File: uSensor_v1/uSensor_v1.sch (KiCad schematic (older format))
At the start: 224 parts, among them J1 +12V Supply, J2 Conn_01x03, J3 Conn_01x03, J4 NS25-W8P 6-pin 2,54mm, J5 USB_B, J6 GNDA-GNDD Jumper, Q1 BC817-25, Q2 BC817-25, SW1 SW_Push, SW2 SW_Push, U1 AM10TW-2405DZ, U10 KSS-213, U11 AD7795, U12 AD5667, U13 TBD, U15 REF192, U2 LD1117A, U22 RCLAMP, U3 STM32F407VGTx, U4 MCP9700AT, U5 MCP9700AT, U6 LM6132A, U7 MCP9700AT, U8 MCP9700AT, U9 UG-2864KSWLG01

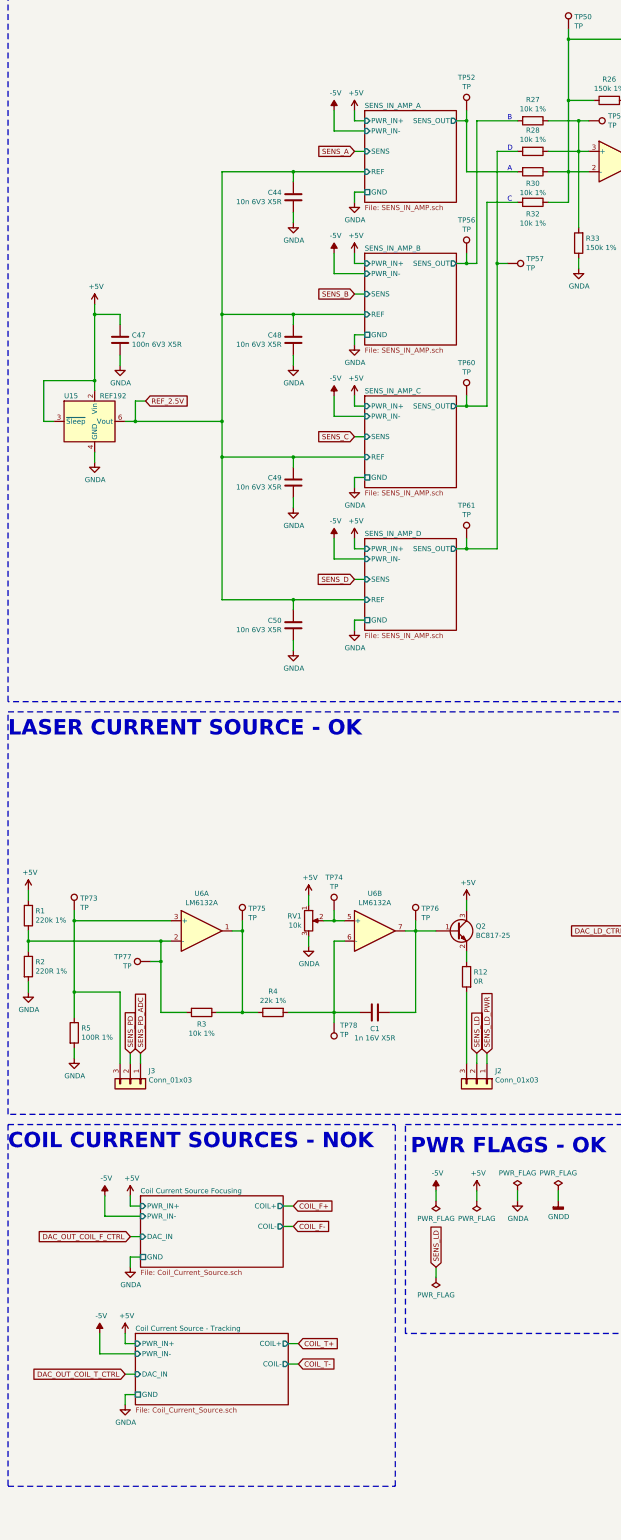
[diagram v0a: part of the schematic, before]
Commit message: Schematic changed (added 2channel opamp in one HS)
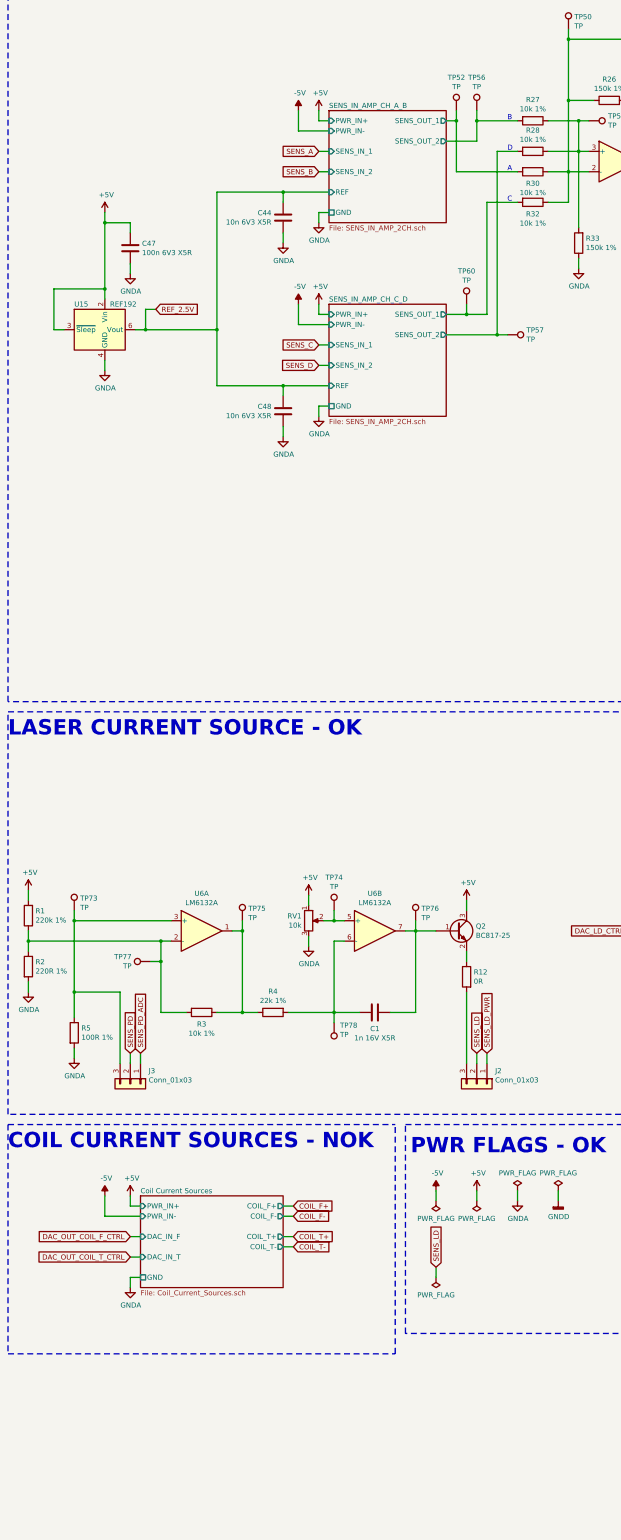
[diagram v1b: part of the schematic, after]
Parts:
- removed C49, C50: 10n 6V3 X5R, Capacitor_SMD:C_0603_1608Metric_Pad1.05x0.95mm_HandSolder, symbol Device:C
- removed TP61: TP, Sentisa-Connectors:TestPoint_Probe_1.0mmDiameter_0.6mmDrill, symbol Connector:TestPoint
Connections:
- net SENS_IN_AMP_A/SENS_OUT renamed SENS_IN_AMP_CH_A_B/SENS_OUT_1
- net SENS_IN_AMP_B/SENS_OUT renamed SENS_IN_AMP_CH_A_B/SENS_OUT_2
- net SENS_IN_AMP_C/SENS_OUT renamed SENS_IN_AMP_CH_C_D/SENS_OUT_1
- net SENS_IN_AMP_D/SENS_OUT renamed SENS_IN_AMP_CH_C_D/SENS_OUT_2
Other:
- moved on the sheet: C47, TP52, TP56, TP57, TP60, U15

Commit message: Layout in progress.
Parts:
- removed C44, C48: 10n 6V3 X5R, Capacitor_SMD:C_0603_1608Metric_Pad1.05x0.95mm_HandSolder, symbol Device:C
- added J7: Barrel_Jack_Switch, Connector_BarrelJack:BarrelJack_Wuerth_6941xx301002, symbol Connector:Barrel_Jack_Switch
- U10: value KSS-213 -> KSS-213 Connector; footprint TBD -> Marcel -> Connector_FFC-FPC:TE_1-84952-6_1x16-1MP_P1.0mm_Horizontal; MFR Sony -> TBD (Sony); MPN KSS-213C -> (TDB) KSS-213C
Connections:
- net at D1.2 (A), J1.1 (Pin_1), TP3.1: now also J7.1
- net at C11.2, C12.2, D3.2 (A2)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: now also J7.2, J7.3
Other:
- moved on the sheet: C1, C11, C12, C19, D1, D3, J1, J2, J3, L2, Q1, Q2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

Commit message: Layout in progress.
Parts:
- added R75: 100k, Resistor_SMD:R_0603_1608Metric_Pad1.05x0.95mm_HandSolder, symbol Device:R
- added SW3: SW_Push, Button_Switch_THT:SW_PUSH_6mm_H4.3mm, symbol Switch:SW_Push
- U10: footprint Connector_FFC-FPC:TE_1-84952-6_1x16-1MP_P1.0mm_Horizontal -> Sentisa-Connectors:Molex_52271-1679_1x16_1mm_Pitch_FFC_FPC_Horizontal_SMT
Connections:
- net +3V3: now also R75.2
- net GNDD: now also SW3.2
- net PROG_~RST: now also R75.1, SW3.1
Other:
- moved on the sheet: C13, C16, C17, C20, C4, C5, C6, C67, C7, C8, D5, D6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

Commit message: Layout in progress.
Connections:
- net FOC_ERR_2_ADC: now also R70.1; no longer R73.1
- net SENS_B: now also R73.1; no longer R68.1
- net SENS_C: now also R74.1; no longer R69.1
- net SENS_D: now also R68.1; no longer R70.1
- net SENS_PD: now also R69.1; no longer R74.1
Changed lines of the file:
@@
 FT
 NoConn ~ 13600 5450
-Text GLabel 12750 13850 0    50   Input ~ 0
+Text GLabel 11200 16850 0    50   Input ~ 0
 FOC_ERR_2_ADC
 $Comp
@@
 Text GLabel 11200 13850 0    50   Input ~ 0
 SENS_A
+Text GLabel 12750 13850 0    50   Input ~ 0
+SENS_B
+Text GLabel 12450 16450 0    50   Input ~ 0
+SENS_C
 Text GLabel 11200 14850 0    50   Input ~ 0
-SENS_B
-Text GLabel 11200 15850 0    50   Input ~ 0
-SENS_C
-Text GLabel 11200 16850 0    50   Input ~ 0
 SENS_D
 Wire Wire Line
@@
 	14750 16250 14750 15950
 Connection ~ 14750 15950
-Text GLabel 12450 16450 0    50   Input ~ 0
+Text GLabel 11200 15850 0    50   Input ~ 0
 SENS_PD
 Wire Wire Line

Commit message: Layout in progress.
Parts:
- removed TP22: TP, Sentisa-Connectors:TestPoint_Probe_1.0mmDiameter_0.6mmDrill, symbol Connector:TestPoint
- added CS1, CS2, CS3: Curr_Sens, Sentisa-Connectors:Current_Sense_Pin_Header_SMD_Pitch1.27mm, symbol Device:Jumper_NC_Small
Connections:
- net ADC_~CS: now also U3.77 (JTDI/SPI3_NSS/I2S3_WS/TIM2_CH1_ETR/SPI1_NSS/EVENTOUT/PA15); no longer U3.66 (I2S_CKIN/MCO2/TIM8_CH4/SDIO_D1/I2C3_SDA/DCMI_D3/TIM3_CH4/EVENTOUT/PC9)
- net COIL_F+: now also CS1.1; no longer U10.13 (F+)
- net COIL_T+: now also CS2.1; no longer U10.14 (T+)
- net DAC_OUT_COIL_F_CTRL: now also U12.1 (VOUT_A); no longer U12.2 (VOUT_B)
- net DAC_OUT_COIL_T_CTRL: now also U12.2 (VOUT_B); no longer U12.1 (VOUT_A)
- net DAC_~LDAC: now also TP21.1
- net SENS_LD: now also CS3.1; no longer L4.1
- net at R9.1, U3.97 (PE0/TIM4_ETR/FSMC_NBL0/DCMI_D2/EVENTOUT): no longer TP21.1
- new net: CS1.2, U10.13 (F+)
- new net: CS3.2, L4.1
- new net: CS2.2, U10.14 (T+)
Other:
- moved on the sheet: C42, L4, TP27, TP28, TP29, TP30, TP31, TP32

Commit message: Connection done.
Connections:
- net +3V3: no longer C21.1, C22.1, C23.1, C24.1, U4.1 (Vdd), U5.1 (Vdd), U7.1 (Vdd), U8.1 (Vdd)
- net +5V: now also C21.1, C22.1, C23.1, C24.1, U4.1 (Vdd), U5.1 (Vdd), U7.1 (Vdd), U8.1 (Vdd)
- net GNDA: now also C21.2, C22.2, C23.2, C24.2, U4.3 (GND), U5.3 (GND), U7.3 (GND), U8.3 (GND)
- net GNDD: no longer C21.2, C22.2, C23.2, C24.2, U4.3 (GND), U5.3 (GND), U7.3 (GND), U8.3 (GND)
- net TEMP_SENS_OUT_1: now also U7.2 (Vout); no longer U4.2 (Vout)
- net TEMP_SENS_OUT_2: now also U4.2 (Vout); no longer U7.2 (Vout)
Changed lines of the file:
@@
 	13200 9900 13200 9800
 $Comp
-L power:+3V3 #PWR08
+L power:+5V #PWR08
 U 1 1 5DA192D4
 P 13200 9000
 F 0 "#PWR08" H 13200 8850 50  0001 C CNN
-F 1 "+3V3" H 13215 9173 50  0000 C CNN
+F 1 "+5V" H 13215 9173 50  0000 C CNN
 F 2 "" H 13200 9000 50  0001 C CNN
 F 3 "" H 13200 9000 50  0001 C CNN
@@
 	13200 9200 13200 9100
 Connection ~ 13200 9100
-Text GLabel 13800 9500 2    40   Output ~ 0
+Text GLabel 13700 11100 2    40   Output ~ 0
 TEMP_SENS_OUT_1
 Wire Wire Line
@@
 $EndComp
 $Comp
-L power:GNDD #PWR017
+L power:GNDA #PWR017
 U 1 1 5DAE0233
 P 13200 11600
 F 0 "#PWR017" H 13200 11350 50  0001 C CNN
-F 1 "GNDD" H 13205 11427 50  0000 C CNN
+F 1 "GNDA" H 13205 11427 50  0000 C CNN
 F 2 "" H 13200 11600 50  0001 C CNN
 F 3 "" H 13200 11600 50  0001 C CNN
@@
 	13200 11500 13200 11400
 $Comp
-L power:+3V3 #PWR015
+L power:+5V #PWR015
 U 1 1 5DAE023E
 P 13200 10600
 F 0 "#PWR015" H 13200 10450 50  0001 C CNN
-F 1 "+3V3" H 13215 10773 50  0000 C CNN
+F 1 "+5V" H 13215 10773 50  0000 C CNN
 F 2 "" H 13200 10600 50  0001 C CNN
 F 3 "" H 13200 10600 50  0001 C CNN
@@
 	13200 10800 13200 10700
 Connection ~ 13200 10700
-Text GLabel 13700 11100 2    40   Output ~ 0
+Text GLabel 13800 9500 2    40   Output ~ 0
 TEMP_SENS_OUT_2
 Wire Wire Line
@@
 	15550 9900 15550 9800
 $Comp
-L power:+3V3 #PWR09
+L power:+5V #PWR09
 U 1 1 5DB14C16
 P 15550 9000
 F 0 "#PWR09" H 15550 8850 50  0001 C CNN
-F 1 "+3V3" H 15565 9173 50  0000 C CNN
+F 1 "+5V" H 15565 9173 50  0000 C CNN
 F 2 "" H 15550 9000 50  0001 C CNN
 F 3 "" H 15550 9000 50  0001 C CNN
@@
 $EndComp
 $Comp
-L power:GNDD #PWR018
+L power:GNDA #PWR018
 U 1 1 5DB14C31
 P 15550 11600
 F 0 "#PWR018" H 15550 11350 50  0001 C CNN
-F 1 "GNDD" H 15555 11427 50  0000 C CNN
+F 1 "GNDA" H 15555 11427 50  0000 C CNN
 F 2 "" H 15550 11600 50  0001 C CNN
 F 3 "" H 15550 11600 50  0001 C CNN
@@
 	15550 11500 15550 11400
 $Comp
-L power:+3V3 #PWR016
+L power:+5V #PWR016
 U 1 1 5DB14C3C
 P 15550 10600
 F 0 "#PWR016" H 15550 10450 50  0001 C CNN
-F 1 "+3V3" H 15565 10773 50  0000 C CNN
+F 1 "+5V" H 15565 10773 50  0000 C CNN
 F 2 "" H 15550 10600 50  0001 C CNN
 F 3 "" H 15550 10600 50  0001 C CNN
@@
 $EndComp
 $Comp
-L power:GNDD #PWR014
+L power:GNDA #PWR014
 U 1 1 5DB14C0B
 P 15550 10000
 F 0 "#PWR014" H 15550 9750 50  0001 C CNN
-F 1 "GNDD" H 15555 9827 50  0000 C CNN
+F 1 "GNDA" H 15555 9827 50  0000 C CNN
 F 2 "" H 15550 10000 50  0001 C CNN
 F 3 "" H 15550 10000 50  0001 C CNN
@@
 $EndComp
 $Comp
-L power:GNDD #PWR0156
+L power:GNDA #PWR0156
 U 1 1 5D33AE3D
 P 13200 10000
 F 0 "#PWR0156" H 13200 9750 50  0001 C CNN
-F 1 "GNDD" H 13204 9845 50  0000 C CNN
+F 1 "GNDA" H 13204 9845 50  0000 C CNN
 F 2 "" H 13200 10000 50  0001 C CNN
 F 3 "" H 13200 10000 50  0001 C CNN

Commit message: Layout ready to 1st review.
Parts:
- J1: footprint Connector_PinHeader_2.54mm:PinHeader_1x02_P2.54mm_Vertical -> Connector_Molex:Molex_KK-254_AE-6410-02A_1x02_P2.54mm_Vertical
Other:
- moved on the sheet: C11, D1, D3, J1, J7, TP3, TP4
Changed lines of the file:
@@
 L Connector_Generic:Conn_01x02 J1
 U 1 1 5C42724A
-P 850 2200
-F 0 "J1" V 1150 2150 50  0000 C CNN
-F 1 "+12V Supply" V 1050 2150 50  0000 C CNN
-F 2 "Connector_PinHeader_2.54mm:PinHeader_1x02_P2.54mm_Vertical" H 850 2200 50  0001 C CNN
-F 3 "~" H 850 2200 50  0001 C CNN
-F 4 "Main Supply Connector" V 950 2150 50  0000 C CNN "Function"
-	1    850  2200
+P 1000 2200
+F 0 "J1" V 1300 2150 50  0000 C CNN
+F 1 "+12V Supply" V 1200 2150 50  0000 C CNN
+F 2 "Connector_Molex:Molex_KK-254_AE-6410-02A_1x02_P2.54mm_Vertical" H 1000 2200 50  0001 C CNN
+F 3 "~" H 1000 2200 50  0001 C CNN
+F 4 "Main Supply Connector" V 1100 2150 50  0000 C CNN "Function"
+	1    1000 2200
 	-1   0    0    -1
 $EndComp
@@
 L Device:C C11
 U 1 1 5C427492
-P 2200 2250
-F 0 "C11" H 2315 2296 50  0000 L CNN
-F 1 "2u2 50V X5R" H 2315 2205 50  0000 L CNN
-F 2 "Resistor_SMD:R_0805_2012Metric_Pad1.15x1.40mm_HandSolder" H 2238 2100 50  0001 C CNN
-F 3 "~" H 2200 2250 50  0001 C CNN
-	1    2200 2250
+P 2250 2250
+F 0 "C11" H 2365 2296 50  0000 L CNN
+F 1 "2u2 50V X5R" H 2365 2205 50  0000 L CNN
+F 2 "Resistor_SMD:R_0805_2012Metric_Pad1.15x1.40mm_HandSolder" H 2288 2100 50  0001 C CNN
+F 3 "~" H 2250 2250 50  0001 C CNN
+	1    2250 2250
 	1    0    0    -1
 $EndComp
@@
 	3000 2500 3000 2400
 Wire Wire Line
-	2200 2500 2200 2400
+	2250 2500 2250 2400
 Wire Wire Line
-	1050 2300 1350 2300
+	1200 2300 1400 2300
 Wire Wire Line
-	1450 2300 1450 2500
-Connection ~ 2200 2500
+	1500 2300 1500 2500
+Connection ~ 2250 2500
 Wire Wire Line
-	1050 2200 1250 2200
+	1200 2200 1300 2200
 Wire Wire Line
-	1450 2200 1450 2000
+	1500 2200 1500 2000
 Wire Wire Line
-	2200 2000 2200 2100
+	2250 2000 2250 2100
 Wire Wire Line
-	2500 2000 2200 2000
+	2500 2000 2250 2000
 Wire Wire Line
 	2800 2000 3000 2000
@@
 L Device:D_Schottky D1
 U 1 1 5CAE2AA1
-P 1700 2000
-F 0 "D1" H 1700 1784 50  0000 C CNN
-F 1 "40V 2A" H 1700 1875 50  0000 C CNN
-F 2 "Sentisa-Diodes:D_SMB" H 1700 2000 50  0001 C CNN
-F 3 "~" H 1700 2000 50  0001 C CNN
-F 4 "Diotec Semiconductor" H 1700 2000 50  0001 C CNN "MFR"
-F 5 "SK25" H 1700 2000 50  0001 C CNN "MPN"
-	1    1700 2000
+P 1750 2000
+F 0 "D1" H 1750 1784 50  0000 C CNN
+F 1 "40V 2A" H 1750 1875 50  0000 C CNN
+F 2 "Sentisa-Diodes:D_SMB" H 1750 2000 50  0001 C CNN
+F 3 "~" H 1750 2000 50  0001 C CNN
+F 4 "Diotec Semiconductor" H 1750 2000 50  0001 C CNN "MFR"
+F 5 "SK25" H 1750 2000 50  0001 C CNN "MPN"
+	1    1750 2000
 	-1   0    0    1
 $EndComp
 Wire Wire Line
-	1850 2000 1950 2000
-Connection ~ 2200 2000
+	1900 2000 2000 2000
+Connection ~ 2250 2000
 $Comp
 L Device:R R6
@@
 L Diode:1.5KExxA D3
 U 1 1 5E6A365E
-P 1950 2250
-F 0 "D3" V 1904 2172 50  0000 R CNN
-F 1 "TVS 40V" V 1995 2172 50  0000 R CNN
-F 2 "Sentisa-Diodes:D_SMB" H 1950 2050 50  0001 C CNN
-F 3 "" H 1900 2250 50  0001 C CNN
-F 4 "Vishay" V 1950 2250 50  0001 C CNN "MPN"
-F 5 "SMBJ40D-M3/H" V 1950 2250 50  0001 C CNN "MFR"
-	1    1950 2250
+P 2000 2250
+F 0 "D3" V 1954 2172 50  0000 R CNN
+F 1 "TVS 40V" V 2045 2172 50  0000 R CNN
+F 2 "Sentisa-Diodes:D_SMB" H 2000 2050 50  0001 C CNN
+F 3 "" H 1950 2250 50  0001 C CNN
+F 4 "Vishay" V 2000 2250 50  0001 C CNN "MPN"
+F 5 "SMBJ40D-M3/H" V 2000 2250 50  0001 C CNN "MFR"
+	1    2000 2250
 	0    1    1    0
 $EndComp
 Wire Wire Line
-	1450 2000 1550 2000
+	1500 2000 1600 2000
 Wire Wire Line
-	1450 2500 1950 2500
+	1500 2500 2000 2500
 Wire Wire Line
-	1950 2100 1950 2000
-Connection ~ 1950 2000
+	2000 2100 2000 2000
+Connection ~ 2000 2000
 Wire Wire Line
-	1950 2000 2200 2000
+	2000 2000 2250 2000
 Wire Wire Line
-	1950 2400 1950 2500
-Connection ~ 1950 2500
+	2000 2400 2000 2500
+Connection ~ 2000 2500
 Text GLabel 8400 14650 2    50   Output ~ 0
 DAC_OUT_COIL_T_CTRL
 Wire Wire Line
-	1950 2500 2200 2500
+	2000 2500 2250 2500
 Wire Wire Line
-	2200 2500 3000 2500
+	2250 2500 3000 2500
 Wire Wire Line
 	20750 5550 20950 5550
@@
 L Connector:TestPoint TP3
 U 1 1 5C3E6779
-P 1450 1900
-F 0 "TP3" H 1450 2225 50  0000 C CNN
-F 1 "TP" H 1450 2134 50  0000 C CNN
-F 2 "Sentisa-Connectors:TestPoint_Probe_1.0mmDiameter_0.6mmDrill" H 1650 1900 50  0001 C CNN
-F 3 "~" H 1650 1900 50  0001 C CNN
-	1    1450 1900
+P 1500 1900
+F 0 "TP3" H 1500 2225 50  0000 C CNN
+F 1 "TP" H 1500 2134 50  0000 C CNN
+F 2 "Sentisa-Connectors:TestPoint_Probe_1.0mmDiameter_0.6mmDrill" H 1700 1900 50  0001 C CNN
+F 3 "~" H 1700 1900 50  0001 C CNN
+	1    1500 1900
 	1    0    0    -1
 $EndComp
@@
 L Connector:TestPoint TP4
 U 1 1 5C459570
-P 1450 2600
-F 0 "TP4" H 1392 2627 50  0000 R CNN
-F 1 "TP" H 1392 2718 50  0000 R CNN
-F 2 "Sentisa-Connectors:TestPoint_Probe_1.0mmDiameter_0.6mmDrill" H 1650 2600 50  0001 C CNN
-F 3 "~" H 1650 2600 50  0001 C CNN
-	1    1450 2600
+P 1500 2600
+F 0 "TP4" H 1442 2627 50  0000 R CNN
+F 1 "TP" H 1442 2718 50  0000 R CNN
+F 2 "Sentisa-Connectors:TestPoint_Probe_1.0mmDiameter_0.6mmDrill" H 1700 2600 50  0001 C CNN
+F 3 "~" H 1700 2600 50  0001 C CNN
+	1    1500 2600
 	-1   0    0    1
 $EndComp
@@
 	9700 24550 9800 24550
 Wire Wire Line
-	1450 2600 1450 2500
-Connection ~ 1450 2500
+	1500 2600 1500 2500
+Connection ~ 1500 2500
 Wire Wire Line
-	1450 1900 1450 2000
-Connection ~ 1450 2000
+	1500 1900 1500 2000
+Connection ~ 1500 2000
 Wire Wire Line
 	7000 1650 7000 1750
@@
 L Connector:Barrel_Jack_Switch J7
 U 1 1 5CBD7599
-P 850 3250
-F 0 "J7" H 905 3567 50  0000 C CNN
-F 1 "Barrel_Jack_Switch" H 905 3476 50  0000 C CNN
-F 2 "Connector_BarrelJack:BarrelJack_Wuerth_6941xx301002" H 900 3210 50  0001 C CNN
-F 3 "~" H 900 3210 50  0001 C CNN
-	1    850  3250
+P 900 3250
+F 0 "J7" H 955 3567 50  0000 C CNN
+F 1 "Barrel_Jack_Switch" H 955 3476 50  0000 C CNN
+F 2 "Connector_BarrelJack:BarrelJack_Wuerth_6941xx301002" H 950 3210 50  0001 C CNN
+F 3 "~" H 950 3210 50  0001 C CNN
+	1    900  3250
 	1    0    0    -1
 $EndComp
 Wire Wire Line
-	1150 3150 1250 3150
+	1200 3150 1300 3150
 Wire Wire Line
-	1250 3150 1250 2200
-Connection ~ 1250 2200
+	1300 3150 1300 2200
+Connection ~ 1300 2200
 Wire Wire Line
-	1250 2200 1450 2200
+	1300 2200 1500 2200
 Wire Wire Line
-	1150 3250 1350 3250
+	1200 3250 1400 3250
 Wire Wire Line
-	1350 3250 1350 2300
-Connection ~ 1350 2300
+	1400 3250 1400 2300
+Connection ~ 1400 2300
 Wire Wire Line
-	1350 2300 1450 2300
+	1400 2300 1500 2300
 Wire Wire Line
-	1150 3350 1350 3350
+	1200 3350 1400 3350
 Wire Wire Line
-	1350 3350 1350 3250
-Connection ~ 1350 3250
+	1400 3350 1400 3250
+Connection ~ 1400 3250
 Wire Wire Line
 	2600 18500 3700 18500
